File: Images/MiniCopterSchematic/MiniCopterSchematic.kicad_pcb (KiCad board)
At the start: 2 copper layers, 78.6 x 58.6 mm, 21 parts, among them M1 MOTOR_DC_1, M2 MOTOR_DC_2, M3 MOTOR_DC_3, M4 MOTOR_DC_4, Q1 FQP20NO6L, Q2 FQP20NO6L, Q3 FQP20NO6L, Q4 FQP20NO6L

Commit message: Working on PCB organizing and putting on text
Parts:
- added kibuzzard-6440AF37: G***, kibuzzard-6440AF37, F.Cu at (90.0, 82.0)
- added kibuzzard-6440AFC4: G***, kibuzzard-6440AFC4, F.Cu at (111.0, 82.0)
- added kibuzzard-6440AFCF: G***, kibuzzard-6440AFCF, F.Cu at (132.0, 103.0)
- added kibuzzard-6440B5BC: G***, kibuzzard-6440B5BC, F.Cu at (81.0, 111.0)
- added kibuzzard-6440B803: G***, kibuzzard-6440B803, F.Cu at (84.0, 127.0)
- added kibuzzard-6440B803: G***, kibuzzard-6440B803, F.Cu at (140.0, 80.0)
- added kibuzzard-6440B803: G***, kibuzzard-6440B803, F.Cu at (146.0, 121.0)
- added kibuzzard-6440B803: G***, kibuzzard-6440B803, F.Cu at (94.0, 79.0)
- added kibuzzard-6440B803: G***, kibuzzard-6440B803, F.Cu at (146.0, 104.0)
- added kibuzzard-6440B803: G***, kibuzzard-6440B803, F.Cu at (78.0, 108.0)
- added kibuzzard-6440B80B: G***, kibuzzard-6440B80B, F.Cu at (108.0, 79.0)
- added kibuzzard-6440B80B: G***, kibuzzard-6440B80B, F.Cu at (146.0, 86.0)
- added kibuzzard-6440B80B: G***, kibuzzard-6440B80B, F.Cu at (146.0, 107.0)
- added kibuzzard-6440B80B: G***, kibuzzard-6440B80B, F.Cu at (78.0, 94.0)
- added kibuzzard-6440B80B: G***, kibuzzard-6440B80B, F.Cu at (122.0, 80.0)
- added kibuzzard-6440B80B: G***, kibuzzard-6440B80B, F.Cu at (98.0, 127.0)
- added kibuzzard-6440BA02: G***, kibuzzard-6440BA02, B.Cu at (131.0, 85.0)
- added kibuzzard-6440BA11: G***, kibuzzard-6440BA11, B.Cu at (141.0, 95.0)
- added kibuzzard-6440D5EF: G***, kibuzzard-6440D5EF, F.Cu at (97.0, 112.0)
- added kibuzzard-6440D61E: G***, kibuzzard-6440D61E, F.Cu at (94.0, 111.0)
- added kibuzzard-6440D635: G***, kibuzzard-6440D635, F.Cu at (91.0, 111.0)
- L1: renamed from LIPO_BATTERY_1; value 3.7V 380 mAH -> LIPO 3.7V 380 mAH
- L2: renamed from LIPO_BATTERY_2; value 3.7V 680 mAH -> LIPO 3.7V 680 mAH
- M1, M2, M3, M4: footprint AA_Custom_Components:PowerPad_Pair_4.0x4.0mm -> AA_Custom_Components:PowerPad_Pair_3.0x3.0mm
- N1: renamed from NRF24L01_1; value BREAKOUT -> NRF24L01_Breakout
- moved L1 15.0 mm to (146.0, 95.0), turned to -90 degrees
- moved M3 9.00 mm to (101.0, 79.0)
- moved L2 4.00 mm to (131.0, 80.0)
- moved R3 3.47 mm to (104.9, 108.8)
- moved M4 3.16 mm to (78.0, 101.0)
- moved R2 1.81 mm to (104.9, 103.2)
- moved R4 1.47 mm to (105.0, 114.5)
- moved U1 1.47 mm to (95.0, 86.5)
- moved M1 1.00 mm to (91.0, 127.0)
- moved Q2 0.98 mm to (91.5, 119.8)
- moved Q1 0.97 mm to (91.5, 115.0)
- moved Q3 0.97 mm to (78.9, 115.0)
- moved Q4 0.97 mm to (78.9, 119.9)
- moved N1 0.96 mm to (133.0, 109.6)
- turned M2 to -90 degrees
- renumbered IMU1 to U1
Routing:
- net MOTOR_3: track 0.00 -> 8.23 mm
- net MOTOR_4: track 0.00 -> 5.64 mm
- net MOTOR_1: track 0.00 -> 5.23 mm
- net MOTOR_2: track 0.00 -> 3.57 mm
- added copper zone on F.Cu, net GND
- removed copper zone on B.Cu, net GND

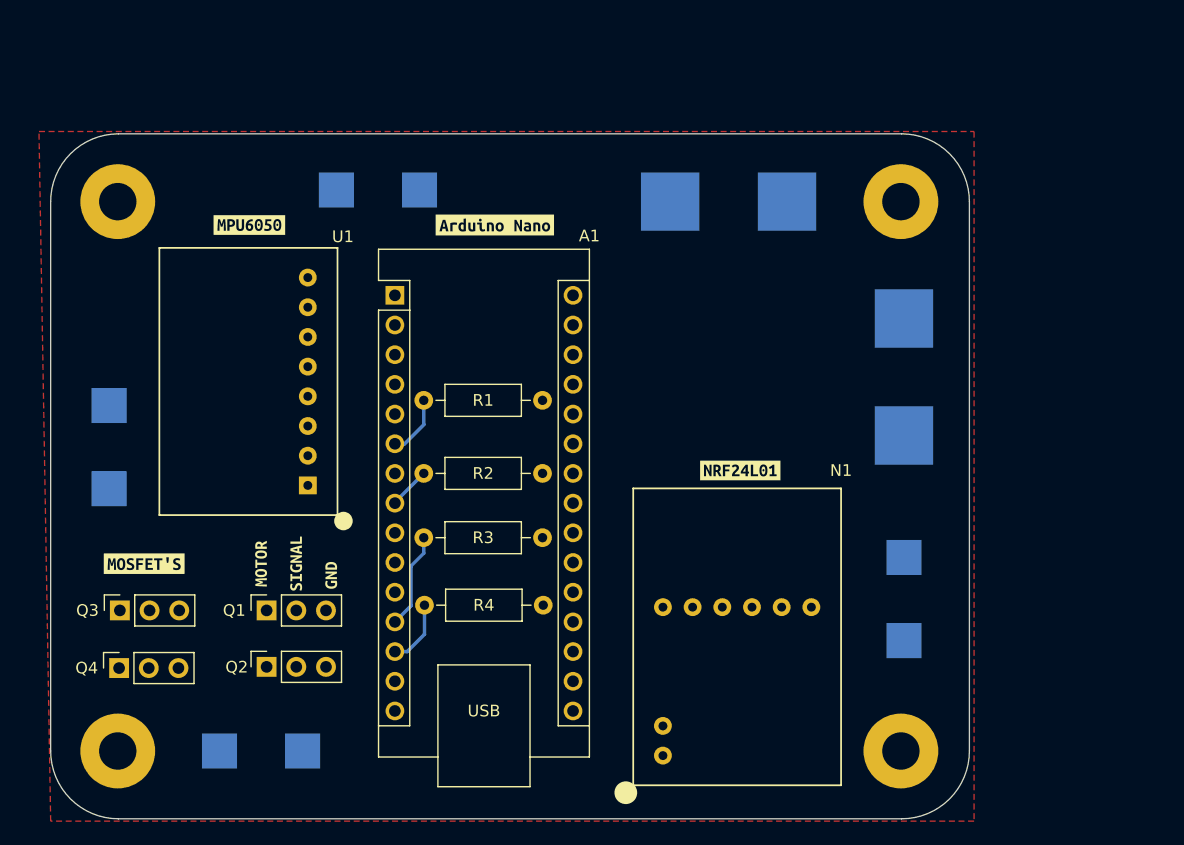
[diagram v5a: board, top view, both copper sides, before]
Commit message: Fixed a lot of errors in the schematic which had caused PCB issues
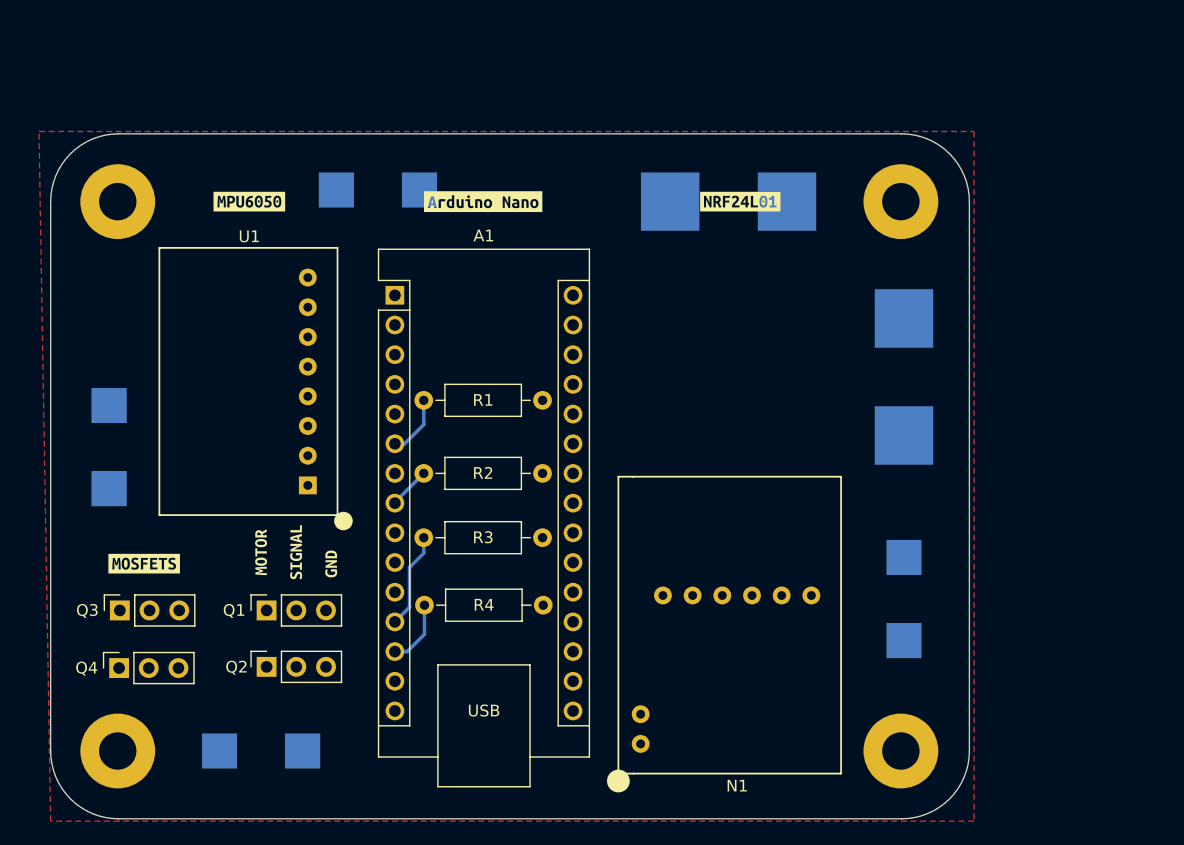
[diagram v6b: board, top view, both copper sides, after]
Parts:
- removed kibuzzard-6440B5BC: G***, kibuzzard-6440B5BC
- added kibuzzard-6440EF4B: G***, kibuzzard-6440EF4B, F.Cu at (81.0, 111.0)
- A1: footprint Module:Arduino_Nano -> AA_Custom_Components:Arduino_Nano
- moved kibuzzard-6440AFCF 23.0 mm to (132.0, 80.0)
- moved kibuzzard-6440AFC4 2.24 mm to (110.0, 80.0)
- moved kibuzzard-6440AF37 2.00 mm to (90.0, 80.0)
- moved N1 1.00 mm to (133.0, 108.6)
- moved kibuzzard-6440D5EF 0.97 mm to (97.0, 111.0)
- moved kibuzzard-6440D61E 0.97 mm to (94.0, 110.0)
- moved kibuzzard-6440D635 0.97 mm to (91.0, 110.0)
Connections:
- A1 pad 27: +BATT -> +5V
- A1 pad 30: +BATT -> +3V3
- L1 pad 1: +BATT -> +3V3
- N1 pad 2: +BATT -> +5V
- U1 pad 1: +BATT -> +5V

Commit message: Working on PCB routing
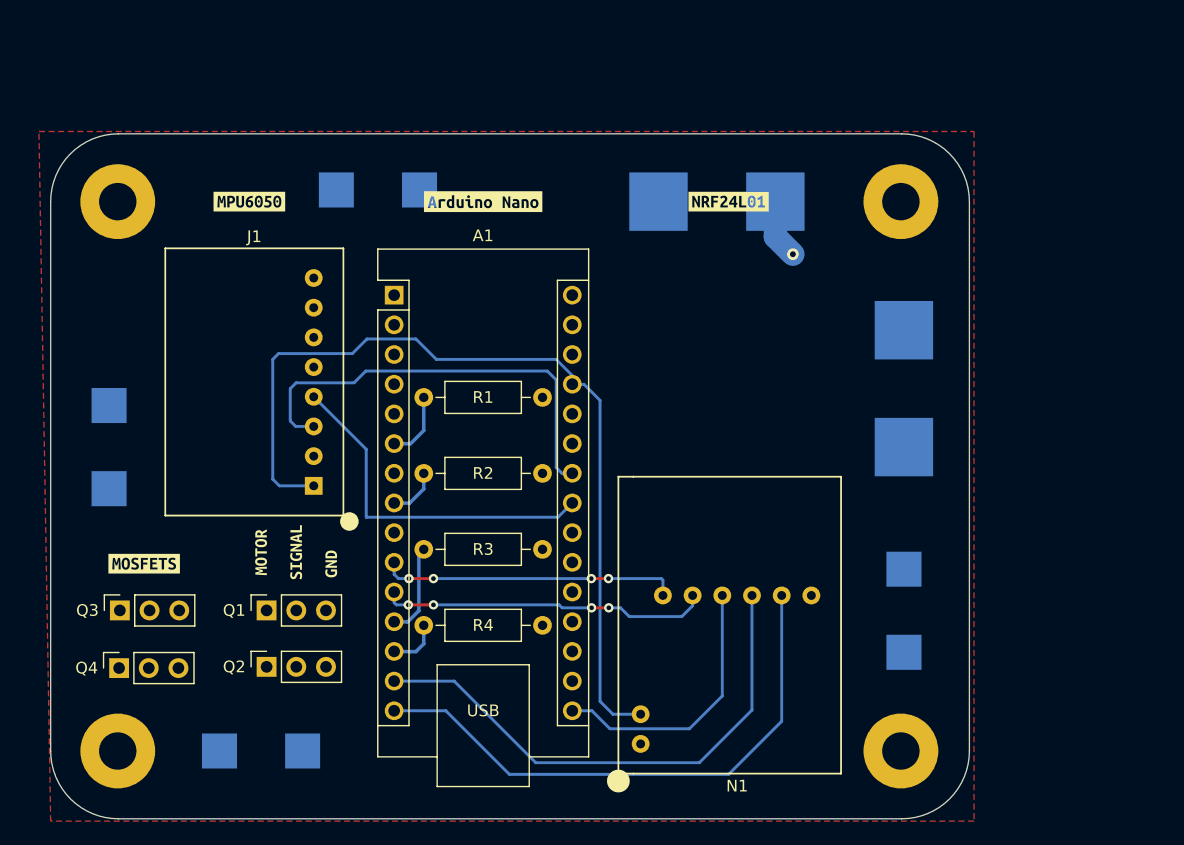
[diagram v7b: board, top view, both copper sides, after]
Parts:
- removed U1: MPU6050, AA_Custom_Components:MPU6050
- added J1: MPU6050, AA_Custom_Components:MPU6050, F.Cu at (95.5, 86.5)
- A1: value ARDUINO NANO EVERY -> ARDUINO NANO
- M1: value MOTOR_DC_1 -> Motor_DC_1
- M2: value MOTOR_DC_2 -> Motor_DC_2
- M3: value MOTOR_DC_3 -> Motor_DC_3
- M4: value MOTOR_DC_4 -> Motor_DC_4
- Q1, Q2, Q3, Q4: footprint Connector_PinSocket_2.54mm:PinSocket_1x03_P2.54mm_Vertical -> AA_Custom_Components:3Pin_MOSFET_MotorDriver
- moved kibuzzard-6440B803 14.0 mm to (98.0, 127.0)
- moved kibuzzard-6440B803 14.0 mm to (108.0, 79.0)
- moved kibuzzard-6440B80B 14.0 mm to (94.0, 79.0)
- moved kibuzzard-6440B80B 14.0 mm to (84.0, 127.0)
- moved R4 1.73 mm to (104.9, 116.2)
- moved kibuzzard-6440B80B 1.50 mm to (120.5, 80.0)
- moved L1 1.00 mm to (146.0, 96.0)
- moved L2 1.00 mm to (130.0, 80.0)
- moved M2 1.00 mm to (146.0, 115.0)
- moved R3 1.00 mm to (104.9, 109.8)
- moved kibuzzard-6440AFCF 1.00 mm to (131.0, 80.0)
- moved kibuzzard-6440B803 1.00 mm to (146.0, 105.0)
- moved kibuzzard-6440BA02 1.00 mm to (130.0, 85.0)
- moved kibuzzard-6440BA11 1.00 mm to (141.0, 96.0)
- moved kibuzzard-6440B803 0.90 mm to (146.0, 121.9)
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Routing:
- net +5V: track 0.00 -> 74.9 mm
- net MISO_NANO: track 0.00 -> 48.1 mm
- net MOSI_NANO: track 0.00 -> 45.2 mm
- net SCL: track 0.00 -> 37.7 mm
- net SDA: track 0.00 -> 30.3 mm
- net CSN_NANO: track 0.00 -> 28.4 mm, vias 0 -> 4
- net CE_NANO: track 0.00 -> 25.5 mm, vias 0 -> 4
- net SCK_NANO: track 0.00 -> 23.2 mm
- net GND: track 0.00 -> 5.12 mm, vias 0 -> 1
- net MOTOR_4: track 5.64 -> 4.33 mm
- net MOTOR_2: track 3.57 -> 4.30 mm
